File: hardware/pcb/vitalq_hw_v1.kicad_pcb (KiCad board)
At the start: 4 copper layers, 36.5 x 53.4 mm, 191 parts, among them J1 USB-C, J2 LiPo pads, J3 FSR pads, J5 ECG pads, J6 EDA pads, J7 Chest bioZ, Q1 CSD13380F3, Q2 CSD13380F3, Q3 BC847BS,115, U1 ESP32-WROOM-32E-N8R2, U10 AS7341-DLGM, U11 TMP117AIDRVR, U12 MLX90632SLD-DCB-100-SP, U13 BME280, U14 LSM6DSV80XTR, U15 TPS61240YFFR, U16 SFH 7072, U17 MAX17048G+T10, U18 W25Q512JVEIQ, U19 TCA6408ARSVR, U2 BQ25170DSGR, U20 TMP117AIDRVR, U3 TPS63802DLAR, U4 TPS7A2018PDBVR, U5 CP2102N-A02-GQFN28R, U6 AFE4900YZR, U7 AD5940BCBZ-RL7, U8 ADS1292RIRSMT, U9 PCA9306DCUR

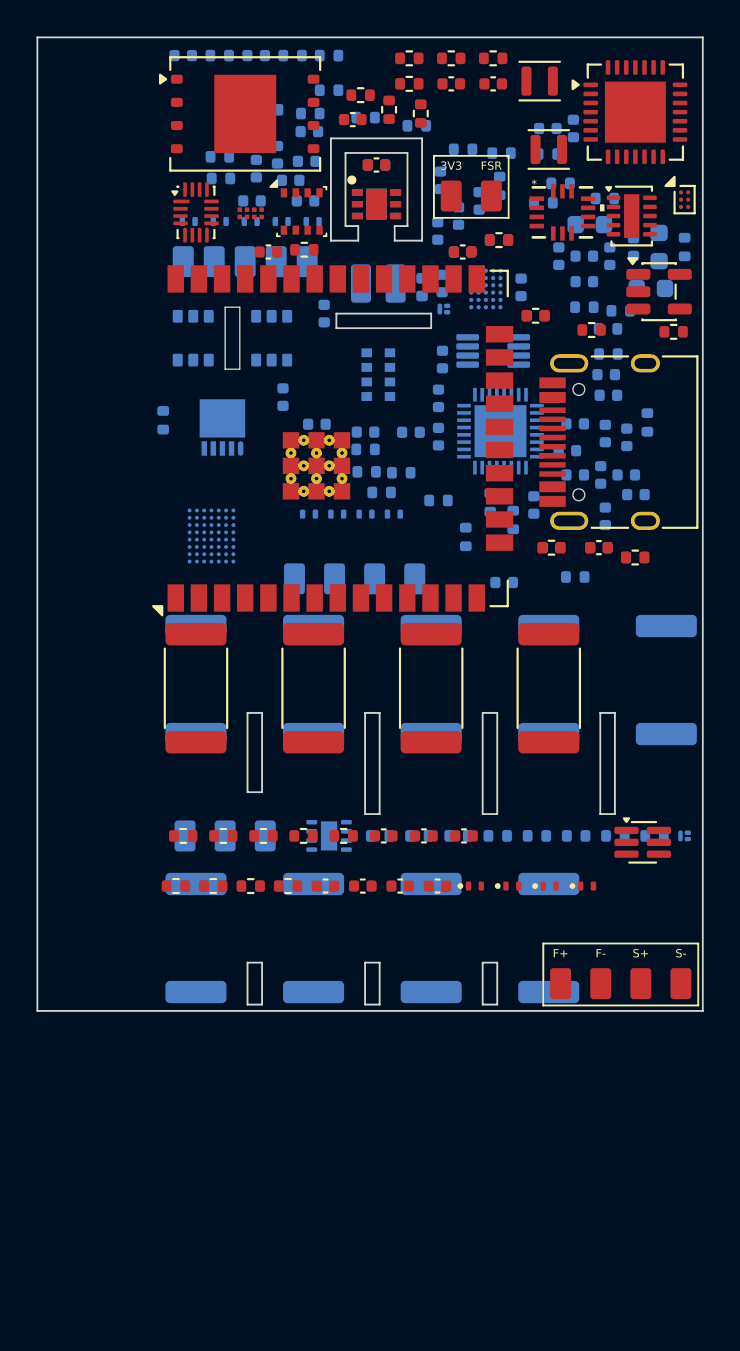
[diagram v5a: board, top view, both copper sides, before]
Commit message: Prepare hw_v1 for prefab review without claiming the route is finished.
Add the gauge TDFN, USB ESD, sense links, test access, and JLC BOM fields, and keep the partial Freerouting result with the remaining open nets listed.

Co-authored-by: Riyu-D1 <Riyu-D1@users.noreply.github.com>
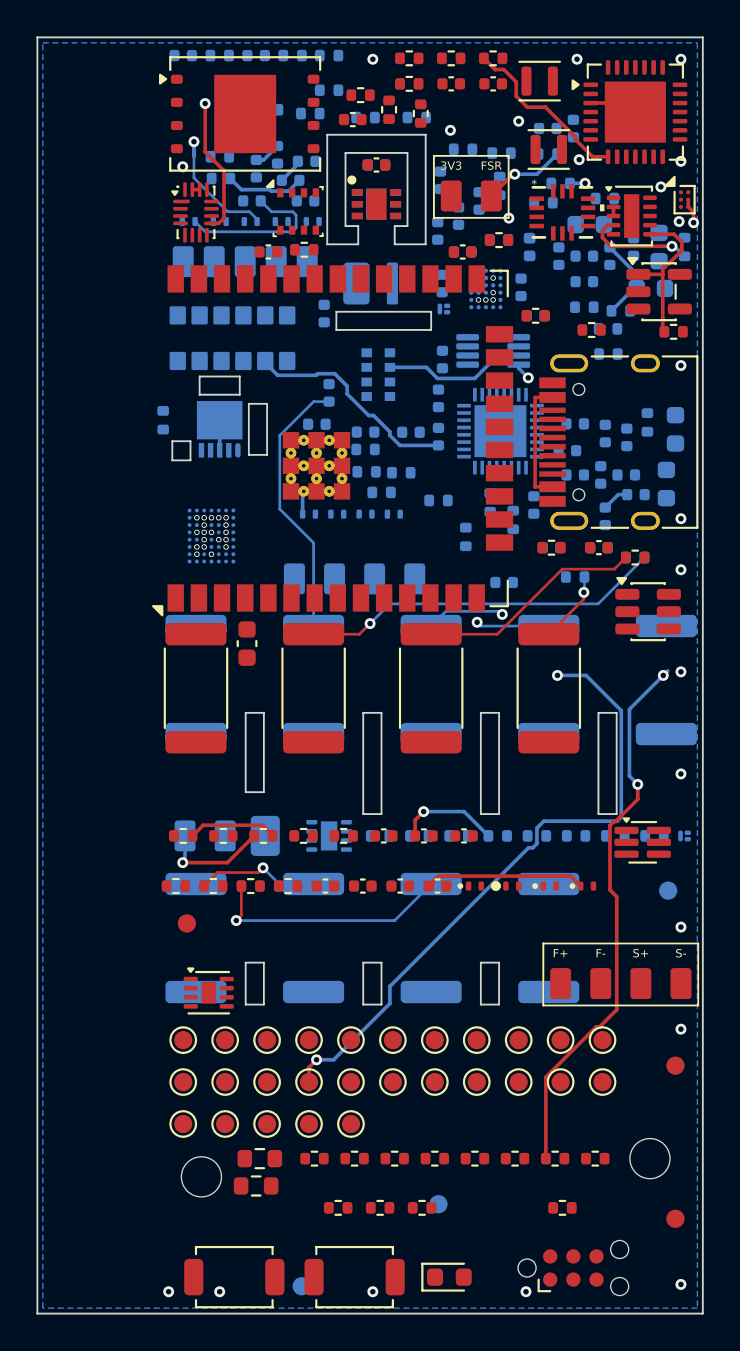
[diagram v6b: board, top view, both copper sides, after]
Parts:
- added D25: KT-0603G, LED_SMD:LED_0603_1608Metric, F.Cu at (22.6, 68.0)
- added FID1: FID, vitalq:Fiducial_1mm, F.Cu at (35.0, 56.4)
- added FID2: FID, vitalq:Fiducial_1mm, F.Cu at (8.20, 48.6)
- added FID3: FID, vitalq:Fiducial_1mm, F.Cu at (35.0, 64.8)
- added FID4: FID, vitalq:Fiducial_1mm, B.Cu at (34.6, 46.8)
- added FID5: FID, vitalq:Fiducial_1mm, B.Cu at (22.0, 64.0)
- added FID6: FID, vitalq:Fiducial_1mm, B.Cu at (14.5, 68.5)
- added H1: M2, MountingHole:MountingHole_2.2mm_M2, B.Cu at (9.00, 62.5)
- added H2: M2, MountingHole:MountingHole_2.2mm_M2, B.Cu at (33.6, 61.5)
- added J8: TC2030, Connector:Tag-Connect_TC2030-IDC-NL_2x03_P1.27mm_Vertical, F.Cu at (29.4, 67.5)
- added R100: 10k, Resistor_SMD:R_0402_1005Metric, F.Cu at (21.1, 64.2)
- added R101: 10k, Resistor_SMD:R_0402_1005Metric, F.Cu at (28.8, 64.2)
- added R88: 1k, Resistor_SMD:R_0402_1005Metric, F.Cu at (15.2, 61.5)
- added R89: 0, Resistor_SMD:R_0402_1005Metric, F.Cu at (17.4, 61.5)
- added R90: 0, Resistor_SMD:R_0402_1005Metric, F.Cu at (19.6, 61.5)
- added R91: 0, Resistor_SMD:R_0402_1005Metric, F.Cu at (21.8, 61.5)
- added R92: 0, Resistor_SMD:R_0402_1005Metric, F.Cu at (24.0, 61.5)
- added R93: 0, Resistor_SMD:R_0603_1608Metric, F.Cu at (12.0, 63.0)
- added R94: 0, Resistor_SMD:R_0603_1608Metric, F.Cu at (12.2, 61.5)
- added R95: 0, Resistor_SMD:R_0402_1005Metric, F.Cu at (26.2, 61.5)
- added R96: 0, Resistor_SMD:R_0402_1005Metric, F.Cu at (28.4, 61.5)
- added R97: 0, Resistor_SMD:R_0402_1005Metric, F.Cu at (30.6, 61.5)
- added R98: 10k, Resistor_SMD:R_0402_1005Metric, F.Cu at (16.5, 64.2)
- added R99: 100k, Resistor_SMD:R_0402_1005Metric, F.Cu at (18.8, 64.2)
- added SW1: TS-1088, Button_Switch_SMD:SW_SPST_TS-1088-xR020, F.Cu at (10.8, 68.0)
- added SW2: TS-1088, Button_Switch_SMD:SW_SPST_TS-1088-xR020, F.Cu at (17.4, 68.0)
- added TP1: VBUS, TestPoint:TestPoint_Pad_D1.0mm, F.Cu at (8.00, 55.0)
- added TP10: ESP_IO0, TestPoint:TestPoint_Pad_D1.0mm, F.Cu at (28.7, 55.0)
- added TP11: ESP_TX, TestPoint:TestPoint_Pad_D1.0mm, F.Cu at (31.0, 55.0)
- added TP12: ESP_RX, TestPoint:TestPoint_Pad_D1.0mm, F.Cu at (8.00, 57.3)
- added TP13: I2C_SDA, TestPoint:TestPoint_Pad_D1.0mm, F.Cu at (10.3, 57.3)
- added TP14: I2C_SCL, TestPoint:TestPoint_Pad_D1.0mm, F.Cu at (12.6, 57.3)
- added TP15: I2C_SDA_1V8, TestPoint:TestPoint_Pad_D1.0mm, F.Cu at (14.9, 57.3)
- added TP16: I2C_SCL_1V8, TestPoint:TestPoint_Pad_D1.0mm, F.Cu at (17.2, 57.3)
- added TP17: SPI_SCK, TestPoint:TestPoint_Pad_D1.0mm, F.Cu at (19.5, 57.3)
- added TP18: SPI_MOSI, TestPoint:TestPoint_Pad_D1.0mm, F.Cu at (21.8, 57.3)
- added TP19: SPI_MISO, TestPoint:TestPoint_Pad_D1.0mm, F.Cu at (24.1, 57.3)
- added TP2: VBAT, TestPoint:TestPoint_Pad_D1.0mm, F.Cu at (10.3, 55.0)
- added TP20: CS_ADS1292, TestPoint:TestPoint_Pad_D1.0mm, F.Cu at (26.4, 57.3)
- added TP21: CS_AFE4900, TestPoint:TestPoint_Pad_D1.0mm, F.Cu at (28.7, 57.3)
- added TP22: CS_AD5940, TestPoint:TestPoint_Pad_D1.0mm, F.Cu at (31.0, 57.3)
- added TP23: CS_FLASH, TestPoint:TestPoint_Pad_D1.0mm, F.Cu at (8.00, 59.6)
- added TP24: ADS1292_DRDY, TestPoint:TestPoint_Pad_D1.0mm, F.Cu at (10.3, 59.6)
- added TP25: AFE4900_ADC_RDY, TestPoint:TestPoint_Pad_D1.0mm, F.Cu at (12.6, 59.6)
- added TP26: EXP_INT, TestPoint:TestPoint_Pad_D1.0mm, F.Cu at (14.9, 59.6)
- added TP27: CHG_STAT, TestPoint:TestPoint_Pad_D1.0mm, F.Cu at (17.2, 59.6)
- added TP3: +3V3, TestPoint:TestPoint_Pad_D1.0mm, F.Cu at (12.6, 55.0)
- added TP4: +1V8, TestPoint:TestPoint_Pad_D1.0mm, F.Cu at (14.9, 55.0)
- added TP5: TX_5V, TestPoint:TestPoint_Pad_D1.0mm, F.Cu at (17.2, 55.0)
- added TP6: VDD_CP2102, TestPoint:TestPoint_Pad_D1.0mm, F.Cu at (19.5, 55.0)
- added TP7: GND, TestPoint:TestPoint_Pad_D1.0mm, F.Cu at (21.8, 55.0)
- added TP8: GND, TestPoint:TestPoint_Pad_D1.0mm, F.Cu at (24.1, 55.0)
- added TP9: ESP_EN, TestPoint:TestPoint_Pad_D1.0mm, F.Cu at (26.4, 55.0)
- added U21: USBLC6-2SC6, Package_TO_SOT_SMD:SOT-23-6, F.Cu at (33.5, 31.5)
- C1, C10: footprint Capacitor_SMD:C_0402_1005Metric -> Capacitor_SMD:C_0603_1608Metric
- C7: value 10u -> 22u; footprint Capacitor_SMD:C_0402_1005Metric -> Capacitor_SMD:C_0603_1608Metric; moved to F.Cu
- Q1, Q2: value CSD13380F3 -> CSD13380F3T
- R3: value 3.0k -> 1.5k
- U11, U20: footprint snap:SON65P200X200X80-7N -> vitalq:TMP117_DRV_NOPASTE
- U17: footprint vitalq:MAX17048_WLP -> Package_DFN_QFN:TDFN-8-1EP_2x2mm_P0.5mm_EP0.8x1.2mm
- moved U17 42.8 mm to (9.40, 52.4)
- moved C7 28.3 mm to (11.5, 33.2), turned to 90 degrees
- moved D11 6.30 mm to (27.0, 11.5)
- moved C10 5.82 mm to (34.5, 24.5), turned to 90 degrees
- moved C1 4.84 mm to (35.0, 21.5), turned to 90 degrees
- moved C51 2.54 mm to (16.0, 19.5)
- moved R26 0.45 mm to (20.8, 4.40)
- moved U13 0.20 mm to (14.3, 9.55)
- moved U12 0.18 mm to (10.0, 21.5)
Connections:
- C11 pad 1: +3V3 -> +3V3_ANA
- C13 pad 1: +3V3 -> +3V3_ANA
- C16 pad 1: +3V3 -> +3V3_ANA
- C18 pad 1: +3V3 -> +3V3_ANA
- C28 pad 1: +3V3 -> +3V3_ANA
- C29 pad 1: +3V3 -> +3V3_ANA
- C43 pad 1: +3V3 -> +3V3_ANA
- C44 pad 1: VBAT -> VBAT_SYS
- C46 pad 1: VBAT -> VBAT_SYS
- C47 pad 1: TX_5V -> TX_5V_RAW
- C6 pad 1: +1V8 -> +1V8_LDO
- C7 pad 1: +3V3 -> +3V3_ESP
- C8 pad 1: +3V3 -> +3V3_ESP
- R12 pad 1: +3V3 -> +3V3_ANA
- R15 pad 1: +3V3 -> +3V3_ANA
- R26 pad 1: +3V3 -> +3V3_ANA
- R28 pad 1: +3V3 -> +3V3_ANA
- U1 pad 2: +3V3 -> +3V3_ESP
- U1 pad 28: unconnected-(U1-IO17-Pad28) -> STATUS_LED
- U15 pad A1: VBAT -> VBAT_SYS
- U15 pad B2: TX_5V -> TX_5V_RAW
- U15 pad C2: TX_5V -> TX_5V_RAW
- U18 pad 2: SPI_MISO -> MISO_FL
- U3 pad 1: VBAT -> VBAT_SYS
- U3 pad 10: VBAT -> VBAT_SYS
- U4 pad 5: +1V8 -> +1V8_LDO
- U6 pad A4: +3V3 -> +3V3_ANA
- U6 pad C1: +3V3 -> +3V3_ANA
- U6 pad C4: +3V3 -> +3V3_ANA
- U6 pad E2: SPI_MISO -> MISO_AFE
- U7 pad A4: +3V3 -> +3V3_ANA
- U7 pad E8: SPI_MISO -> MISO_AD
- U7 pad F2: +3V3 -> +3V3_ANA
- U7 pad F3: +3V3 -> +3V3_ANA
- U8 pad 12: +3V3 -> +3V3_ANA
- U8 pad 14: +3V3 -> +3V3_ANA
- U8 pad 21: SPI_MISO -> MISO_ADS
- U8 pad 23: +3V3 -> +3V3_ANA
- U8 pad 25: unconnected-(U8-GPIO2/RCLK2-Pad25) -> ADS_GPIO2
- U8 pad 26: unconnected-(U8-GPIO1/RCLK1-Pad26) -> ADS_GPIO1
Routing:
- net TX_5V_RAW: track 0.00 -> 58.3 mm, vias 0 -> 3
- net RLD_CLAMP: track 0.00 -> 56.5 mm, vias 0 -> 3
- net I2C_SDA_1V8: track 0.00 -> 52.7 mm, vias 0 -> 3
- net GND: track 0.00 -> 43.9 mm, vias 0 -> 25
- net AFE_P_AC: track 0.00 -> 31.7 mm, vias 0 -> 3
- net VBUS_DET: track 0.00 -> 31.3 mm, vias 0 -> 2
- net SE_SURGE: track 0.00 -> 19.9 mm, vias 0 -> 1
- net ECG_N: track 0.00 -> 14.7 mm
- net SP_SURGE: track 0.00 -> 13.5 mm, vias 0 -> 1
- net RE_SURGE: track 0.00 -> 12.4 mm
- net TX_5V: track 0.00 -> 11.9 mm
- net CP_VBUS: track 0.00 -> 9.58 mm
- net +3V3: track 0.00 -> 9.10 mm
- net ECG_P: track 0.00 -> 8.83 mm
- net SN_ISO: track 0.00 -> 8.78 mm
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- added copper zone on In2.Cu, net +1V8
- added copper zone on In2.Cu, net +3V3
- added copper zone on B.Cu, net GND
- added copper zone on In1.Cu, net GND
- added copper zone on In2.Cu, net TX_5V
- added copper zone on In2.Cu, net VBAT
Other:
- board size 36.5 x 53.4 mm -> 36.5 x 70 mm
- board text added: "JLCJLCJLCJLC"
